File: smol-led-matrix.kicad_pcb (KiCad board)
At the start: 4 copper layers, 61.8 x 88.2 mm, 1139 parts, among them J1 USB_C_Receptacle_USB2.0, J2 TagConnect_TC2030_SWD, Q1 FS8205, Q2 AO3401A, SW1 SW_Push, SW2 SW_Push, U1 STM32L433CBTx, U2 TP4054, U3 DW01+G, U4 XC6206P332MR

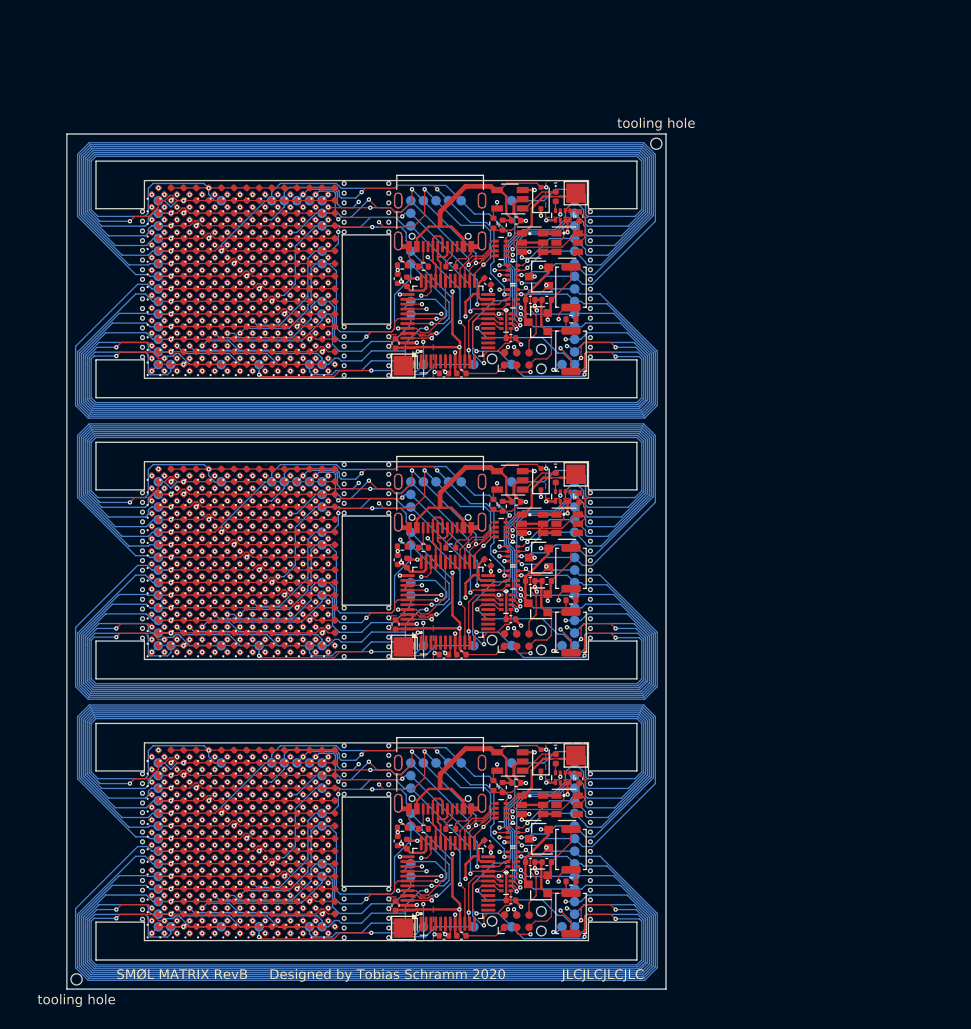
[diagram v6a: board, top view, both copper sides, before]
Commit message: Fix some clearance issues
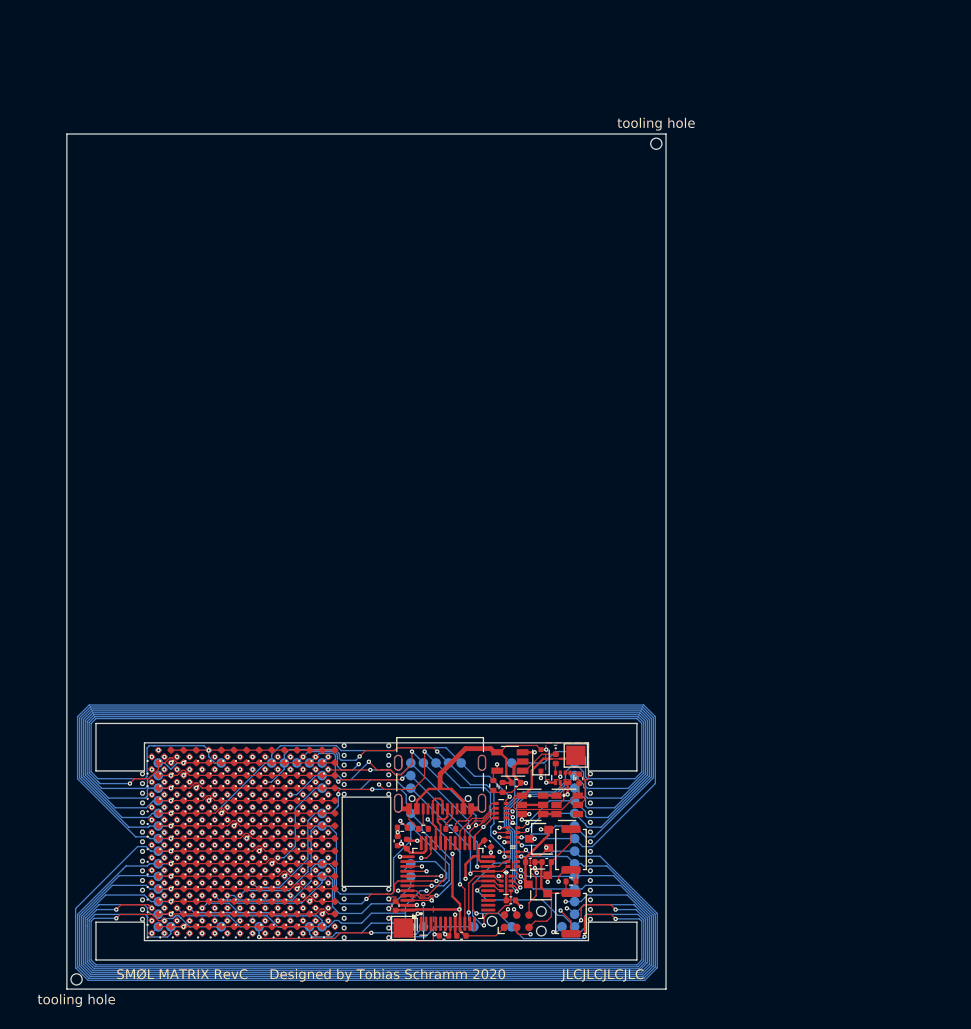
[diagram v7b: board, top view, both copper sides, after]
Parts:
- removed the C1 at (94.8, 86.5)
- removed the C1 at (94.8, 115.5)
- removed the C10 at (99.9, 82.8)
- removed the C10 at (99.9, 111.8)
- removed the C11 at (88.2, 76.7)
- removed the C11 at (88.2, 105.7)
- removed the C2 at (88.0, 83.4)
- removed the C2 at (88.0, 112.4)
- removed the C3 at (100.5, 70.7)
- removed the C3 at (100.5, 99.7)
- removed the C4 at (107.0, 70.3)
- removed the C4 at (107.0, 99.3)
- removed the C5 at (93.0, 86.5)
- removed the C5 at (93.0, 115.5)
- removed the C6 at (101.9, 78.9)
- removed the C6 at (101.9, 107.9)
- removed the C7 at (103.6, 78.9)
- removed the C7 at (103.6, 107.9)
- removed the C8 at (89.2, 77.0)
- removed the C8 at (89.2, 106.0)
- removed the C9 at (97.5, 77.0)
- removed the C9 at (97.5, 106.0)
- removed the D1 at (63.2, 67.7)
- removed the D1 at (63.2, 96.7)
- removed the D10 at (63.2, 79.4)
- removed the D10 at (63.2, 108.4)
- removed the D100 at (71.0, 79.4)
- removed the D100 at (71.0, 108.4)
- removed the D101 at (71.0, 80.7)
- removed the D101 at (71.0, 109.7)
- removed the D102 at (71.0, 82.0)
- removed the D102 at (71.0, 111.0)
- removed the D103 at (71.0, 83.3)
- removed the D103 at (71.0, 112.3)
- removed the D104 at (71.0, 84.6)
- removed the D104 at (71.0, 113.6)
- removed the D105 at (71.0, 85.9)
- removed the D105 at (71.0, 114.9)
- removed the D106 at (72.3, 67.7)
- removed the D106 at (72.3, 96.7)
- removed the D107 at (72.3, 69.0)
- removed the D107 at (72.3, 98.0)
- removed the D108 at (72.3, 70.3)
- removed the D108 at (72.3, 99.3)
- removed the D109 at (72.3, 71.6)
- removed the D109 at (72.3, 100.6)
- removed the D11 at (63.2, 80.7)
- removed the D11 at (63.2, 109.7)
- removed the D110 at (72.3, 72.9)
- removed the D110 at (72.3, 101.9)
- removed the D111 at (72.3, 74.2)
- removed the D111 at (72.3, 103.2)
- removed the D112 at (72.3, 75.5)
- removed the D112 at (72.3, 104.5)
- removed the D113 at (72.3, 76.8)
- removed the D113 at (72.3, 105.8)
- removed the D114 at (72.3, 78.1)
- removed the D114 at (72.3, 107.1)
- removed the D115 at (72.3, 79.4)
- removed the D115 at (72.3, 108.4)
- removed the D116 at (72.3, 80.7)
- removed the D116 at (72.3, 109.7)
- removed the D117 at (72.3, 82.0)
- removed the D117 at (72.3, 111.0)
- removed the D118 at (72.3, 83.3)
- removed the D118 at (72.3, 112.3)
- removed the D119 at (72.3, 84.6)
- removed the D119 at (72.3, 113.6)
- removed the D12 at (63.2, 82.0)
- removed the D12 at (63.2, 111.0)
- removed the D120 at (72.3, 85.9)
- removed the D120 at (72.3, 114.9)
- removed the D121 at (73.6, 67.7)
- removed the D121 at (73.6, 96.7)
- removed the D122 at (73.6, 69.0)
- removed the D122 at (73.6, 98.0)
- removed the D123 at (73.6, 70.3)
- removed the D123 at (73.6, 99.3)
- removed the D124 at (73.6, 71.6)
- removed the D124 at (73.6, 100.6)
- removed the D125 at (73.6, 72.9)
- removed the D125 at (73.6, 101.9)
- removed the D126 at (73.6, 74.2)
- removed the D126 at (73.6, 103.2)
- removed the D127 at (73.6, 75.5)
- removed the D127 at (73.6, 104.5)
- removed the D128 at (73.6, 76.8)
- removed the D128 at (73.6, 105.8)
- removed the D129 at (73.6, 78.1)
- removed the D129 at (73.6, 107.1)
- removed the D13 at (63.2, 83.3)
- removed the D13 at (63.2, 112.3)
- removed the D130 at (73.6, 79.4)
- removed the D130 at (73.6, 108.4)
- removed the D131 at (73.6, 80.7)
- removed the D131 at (73.6, 109.7)
- removed the D132 at (73.6, 82.0)
- removed the D132 at (73.6, 111.0)
- removed the D133 at (73.6, 83.3)
- removed the D133 at (73.6, 112.3)
- removed the D134 at (73.6, 84.6)
- removed the D134 at (73.6, 113.6)
- removed the D135 at (73.6, 85.9)
- removed the D135 at (73.6, 114.9)
- removed the D136 at (74.9, 67.7)
- removed the D136 at (74.9, 96.7)
- removed the D137 at (74.9, 69.0)
- removed the D137 at (74.9, 98.0)
- removed the D138 at (74.9, 70.3)
- removed the D138 at (74.9, 99.3)
- removed the D139 at (74.9, 71.6)
- removed the D139 at (74.9, 100.6)
- removed the D14 at (63.2, 84.6)
- removed the D14 at (63.2, 113.6)
- removed the D140 at (74.9, 72.9)
- removed the D140 at (74.9, 101.9)
- removed the D141 at (74.9, 74.2)
- removed the D141 at (74.9, 103.2)
- removed the D142 at (74.9, 75.5)
- removed the D142 at (74.9, 104.5)
- removed the D143 at (74.9, 76.8)
- removed the D143 at (74.9, 105.8)
- removed the D144 at (74.9, 78.1)
- removed the D144 at (74.9, 107.1)
- removed the D145 at (74.9, 79.4)
- removed the D145 at (74.9, 108.4)
- removed the D146 at (74.9, 80.7)
- removed the D146 at (74.9, 109.7)
- removed the D147 at (74.9, 82.0)
- removed the D147 at (74.9, 111.0)
- removed the D148 at (74.9, 83.3)
- removed the D148 at (74.9, 112.3)
- removed the D149 at (74.9, 84.6)
- removed the D149 at (74.9, 113.6)
- removed the D15 at (63.2, 85.9)
- removed the D15 at (63.2, 114.9)
- removed the D150 at (74.9, 85.9)
- removed the D150 at (74.9, 114.9)
- removed the D151 at (76.2, 67.7)
- removed the D151 at (76.2, 96.7)
- removed the D152 at (76.2, 69.0)
- removed the D152 at (76.2, 98.0)
- removed the D153 at (76.2, 70.3)
- removed the D153 at (76.2, 99.3)
- removed the D154 at (76.2, 71.6)
- removed the D154 at (76.2, 100.6)
- removed the D155 at (76.2, 72.9)
- removed the D155 at (76.2, 101.9)
- removed the D156 at (76.2, 74.2)
- removed the D156 at (76.2, 103.2)
- removed the D157 at (76.2, 75.5)
- removed the D157 at (76.2, 104.5)
- removed the D158 at (76.2, 76.8)
- removed the D158 at (76.2, 105.8)
- removed the D159 at (76.2, 78.1)
- removed the D159 at (76.2, 107.1)
- removed the D16 at (64.5, 67.7)
- removed the D16 at (64.5, 96.7)
- removed the D160 at (76.2, 79.4)
- removed the D160 at (76.2, 108.4)
- removed the D161 at (76.2, 80.7)
- removed the D161 at (76.2, 109.7)
- removed the D162 at (76.2, 82.0)
- removed the D162 at (76.2, 111.0)
- removed the D163 at (76.2, 83.3)
- removed the D163 at (76.2, 112.3)
- removed the D164 at (76.2, 84.6)
- removed the D164 at (76.2, 113.6)
- removed the D165 at (76.2, 85.9)
- removed the D165 at (76.2, 114.9)
- removed the D166 at (77.5, 67.7)
- removed the D166 at (77.5, 96.7)
- removed the D167 at (77.5, 69.0)
- removed the D167 at (77.5, 98.0)
- removed the D168 at (77.5, 70.3)
- removed the D168 at (77.5, 99.3)
- removed the D169 at (77.5, 71.6)
- removed the D169 at (77.5, 100.6)
- removed the D17 at (64.5, 69.0)
- removed the D17 at (64.5, 98.0)
- removed the D170 at (77.5, 72.9)
- removed the D170 at (77.5, 101.9)
- removed the D171 at (77.5, 74.2)
- removed the D171 at (77.5, 103.2)
- removed the D172 at (77.5, 75.5)
- removed the D172 at (77.5, 104.5)
- removed the D173 at (77.5, 76.8)
- removed the D173 at (77.5, 105.8)
- removed the D174 at (77.5, 78.1)
- removed the D174 at (77.5, 107.1)
- removed the D175 at (77.5, 79.4)
- removed the D175 at (77.5, 108.4)
- removed the D176 at (77.5, 80.7)
- removed the D176 at (77.5, 109.7)
- removed the D177 at (77.5, 82.0)
- removed the D177 at (77.5, 111.0)
- removed the D178 at (77.5, 83.3)
- removed the D178 at (77.5, 112.3)
- removed the D179 at (77.5, 84.6)
- removed the D179 at (77.5, 113.6)
- removed the D18 at (64.5, 70.3)
- removed the D18 at (64.5, 99.3)
- removed the D180 at (77.5, 85.9)
- removed the D180 at (77.5, 114.9)
- removed the D181 at (78.8, 67.7)
- removed the D181 at (78.8, 96.7)
- removed the D182 at (78.8, 69.0)
- removed the D182 at (78.8, 98.0)
- removed the D183 at (78.8, 70.3)
- removed the D183 at (78.8, 99.3)
- removed the D184 at (78.8, 71.6)
- removed the D184 at (78.8, 100.6)
- removed the D185 at (78.8, 72.9)
- removed the D185 at (78.8, 101.9)
- removed the D186 at (78.8, 74.2)
- removed the D186 at (78.8, 103.2)
- removed the D187 at (78.8, 75.5)
- removed the D187 at (78.8, 104.5)
- removed the D188 at (78.8, 76.8)
- removed the D188 at (78.8, 105.8)
- removed the D189 at (78.8, 78.1)
- removed the D189 at (78.8, 107.1)
- removed the D19 at (64.5, 71.6)
- removed the D19 at (64.5, 100.6)
- removed the D190 at (78.8, 79.4)
- removed the D190 at (78.8, 108.4)
- removed the D191 at (78.8, 80.7)
- removed the D191 at (78.8, 109.7)
- removed the D192 at (78.8, 82.0)
- removed the D192 at (78.8, 111.0)
- removed the D193 at (78.8, 83.3)
- removed the D193 at (78.8, 112.3)
- removed the D194 at (78.8, 84.6)
- removed the D194 at (78.8, 113.6)
- removed the D195 at (78.8, 85.9)
- removed the D195 at (78.8, 114.9)
- removed the D196 at (80.1, 67.7)
- removed the D196 at (80.1, 96.7)
- removed the D197 at (80.1, 69.0)
- removed the D197 at (80.1, 98.0)
- removed the D198 at (80.1, 70.3)
- removed the D198 at (80.1, 99.3)
- removed the D199 at (80.1, 71.6)
- removed the D199 at (80.1, 100.6)
- removed the D2 at (63.2, 69.0)
- removed the D2 at (63.2, 98.0)
- removed the D20 at (64.5, 72.9)
- removed the D20 at (64.5, 101.9)
- removed the D200 at (80.1, 72.9)
- removed the D200 at (80.1, 101.9)
- removed the D201 at (80.1, 74.2)
- removed the D201 at (80.1, 103.2)
- removed the D202 at (80.1, 75.5)
- removed the D202 at (80.1, 104.5)
- removed the D203 at (80.1, 76.8)
- removed the D203 at (80.1, 105.8)
- removed the D204 at (80.1, 78.1)
- removed the D204 at (80.1, 107.1)
- removed the D205 at (80.1, 79.4)
- removed the D205 at (80.1, 108.4)
- removed the D206 at (80.1, 80.7)
- removed the D206 at (80.1, 109.7)
- removed the D207 at (80.1, 82.0)
- removed the D207 at (80.1, 111.0)
- removed the D208 at (80.1, 83.3)
- removed the D208 at (80.1, 112.3)
- removed the D209 at (80.1, 84.6)
- removed the D209 at (80.1, 113.6)
- removed the D21 at (64.5, 74.2)
- removed the D21 at (64.5, 103.2)
- removed the D210 at (80.1, 85.9)
- removed the D210 at (80.1, 114.9)
- removed the D211 at (81.4, 67.7)
- removed the D211 at (81.4, 96.7)
- removed the D212 at (81.4, 69.0)
- removed the D212 at (81.4, 98.0)
- removed the D213 at (81.4, 70.3)
- removed the D213 at (81.4, 99.3)
- removed the D214 at (81.4, 71.6)
- removed the D214 at (81.4, 100.6)
- removed the D215 at (81.4, 72.9)
- removed the D215 at (81.4, 101.9)
- removed the D216 at (81.4, 74.2)
- removed the D216 at (81.4, 103.2)
- removed the D217 at (81.4, 75.5)
- removed the D217 at (81.4, 104.5)
- removed the D218 at (81.4, 76.8)
- removed the D218 at (81.4, 105.8)
- removed the D219 at (81.4, 78.1)
- removed the D219 at (81.4, 107.1)
- removed the D22 at (64.5, 75.5)
- removed the D22 at (64.5, 104.5)
- removed the D220 at (81.4, 79.4)
- removed the D220 at (81.4, 108.4)
- removed the D221 at (81.4, 80.7)
- removed the D221 at (81.4, 109.7)
- removed the D222 at (81.4, 82.0)
- removed the D222 at (81.4, 111.0)
- removed the D223 at (81.4, 83.3)
- removed the D223 at (81.4, 112.3)
- removed the D224 at (81.4, 84.6)
- removed the D224 at (81.4, 113.6)
- removed the D225 at (81.4, 85.9)
- removed the D225 at (81.4, 114.9)
- removed the D226 at (104.5, 68.2)
- removed the D226 at (104.5, 97.2)
- removed the D227 at (103.0, 68.4)
- removed the D227 at (103.0, 97.4)
- removed the D23 at (64.5, 76.8)
- removed the D23 at (64.5, 105.8)
- removed the D24 at (64.5, 78.1)
- removed the D24 at (64.5, 107.1)
- removed the D25 at (64.5, 79.4)
- removed the D25 at (64.5, 108.4)
- removed the D26 at (64.5, 80.7)
- removed the D26 at (64.5, 109.7)
- removed the D27 at (64.5, 82.0)
- removed the D27 at (64.5, 111.0)
- removed the D28 at (64.5, 83.3)
- removed the D28 at (64.5, 112.3)
- removed the D29 at (64.5, 84.6)
- removed the D29 at (64.5, 113.6)
- removed the D3 at (63.2, 70.3)
- removed the D3 at (63.2, 99.3)
- removed the D30 at (64.5, 85.9)
- removed the D30 at (64.5, 114.9)
- removed the D31 at (65.8, 67.7)
- removed the D31 at (65.8, 96.7)
- removed the D32 at (65.8, 69.0)
- removed the D32 at (65.8, 98.0)
- removed the D33 at (65.8, 70.3)
- removed the D33 at (65.8, 99.3)
- removed the D34 at (65.8, 71.6)
- removed the D34 at (65.8, 100.6)
- removed the D35 at (65.8, 72.9)
- removed the D35 at (65.8, 101.9)
- removed the D36 at (65.8, 74.2)
- removed the D36 at (65.8, 103.2)
- removed the D37 at (65.8, 75.5)
- removed the D37 at (65.8, 104.5)
- removed the D38 at (65.8, 76.8)
- removed the D38 at (65.8, 105.8)
- removed the D39 at (65.8, 78.1)
- removed the D39 at (65.8, 107.1)
- removed the D4 at (63.2, 71.6)
- removed the D4 at (63.2, 100.6)
- removed the D40 at (65.8, 79.4)
- removed the D40 at (65.8, 108.4)
- removed the D41 at (65.8, 80.7)
- removed the D41 at (65.8, 109.7)
- removed the D42 at (65.8, 82.0)
- removed the D42 at (65.8, 111.0)
- removed the D43 at (65.8, 83.3)
- removed the D43 at (65.8, 112.3)
- removed the D44 at (65.8, 84.6)
- removed the D44 at (65.8, 113.6)
- removed the D45 at (65.8, 85.9)
- removed the D45 at (65.8, 114.9)
- removed the D46 at (67.1, 67.7)
- removed the D46 at (67.1, 96.7)
- removed the D47 at (67.1, 69.0)
- removed the D47 at (67.1, 98.0)
- removed the D48 at (67.1, 70.3)
- removed the D48 at (67.1, 99.3)
- removed the D49 at (67.1, 71.6)
- removed the D49 at (67.1, 100.6)
- removed the D5 at (63.2, 72.9)
- removed the D5 at (63.2, 101.9)
- removed the D50 at (67.1, 72.9)
- removed the D50 at (67.1, 101.9)
- removed the D51 at (67.1, 74.2)
- removed the D51 at (67.1, 103.2)
- removed the D52 at (67.1, 75.5)
- removed the D52 at (67.1, 104.5)
- removed the D53 at (67.1, 76.8)
- removed the D53 at (67.1, 105.8)
- removed the D54 at (67.1, 78.1)
- removed the D54 at (67.1, 107.1)
- removed the D55 at (67.1, 79.4)
- removed the D55 at (67.1, 108.4)
- removed the D56 at (67.1, 80.7)
- removed the D56 at (67.1, 109.7)
- removed the D57 at (67.1, 82.0)
- removed the D57 at (67.1, 111.0)
- removed the D58 at (67.1, 83.3)
- removed the D58 at (67.1, 112.3)
- removed the D59 at (67.1, 84.6)
- removed the D59 at (67.1, 113.6)
- removed the D6 at (63.2, 74.2)
- removed the D6 at (63.2, 103.2)
- removed the D60 at (67.1, 85.9)
- removed the D60 at (67.1, 114.9)
- removed the D61 at (68.4, 67.7)
- removed the D61 at (68.4, 96.7)
- removed the D62 at (68.4, 69.0)
- removed the D62 at (68.4, 98.0)
- removed the D63 at (68.4, 70.3)
- removed the D63 at (68.4, 99.3)
- removed the D64 at (68.4, 71.6)
- removed the D64 at (68.4, 100.6)
- removed the D65 at (68.4, 72.9)
- removed the D65 at (68.4, 101.9)
- removed the D66 at (68.4, 74.2)
- removed the D66 at (68.4, 103.2)
- removed the D67 at (68.4, 75.5)
- removed the D67 at (68.4, 104.5)
- removed the D68 at (68.4, 76.8)
- removed the D68 at (68.4, 105.8)
- removed the D69 at (68.4, 78.1)
- removed the D69 at (68.4, 107.1)
- removed the D7 at (63.2, 75.5)
- removed the D7 at (63.2, 104.5)
- removed the D70 at (68.4, 79.4)
- removed the D70 at (68.4, 108.4)
- removed the D71 at (68.4, 80.7)
- removed the D71 at (68.4, 109.7)
- removed the D72 at (68.4, 82.0)
- removed the D72 at (68.4, 111.0)
- removed the D73 at (68.4, 83.3)
- removed the D73 at (68.4, 112.3)
- removed the D74 at (68.4, 84.6)
- removed the D74 at (68.4, 113.6)
- removed the D75 at (68.4, 85.9)
- removed the D75 at (68.4, 114.9)
- removed the D76 at (69.7, 67.7)
- removed the D76 at (69.7, 96.7)
- removed the D77 at (69.7, 69.0)
- removed the D77 at (69.7, 98.0)
- removed the D78 at (69.7, 70.3)
- removed the D78 at (69.7, 99.3)
- removed the D79 at (69.7, 71.6)
- removed the D79 at (69.7, 100.6)
- removed the D8 at (63.2, 76.8)
- removed the D8 at (63.2, 105.8)
- removed the D80 at (69.7, 72.9)
- removed the D80 at (69.7, 101.9)
- removed the D81 at (69.7, 74.2)
- removed the D81 at (69.7, 103.2)
- removed the D82 at (69.7, 75.5)
- removed the D82 at (69.7, 104.5)
- removed the D83 at (69.7, 76.8)
- removed the D83 at (69.7, 105.8)
- removed the D84 at (69.7, 78.1)
- removed the D84 at (69.7, 107.1)
- removed the D85 at (69.7, 79.4)
- removed the D85 at (69.7, 108.4)
- removed the D86 at (69.7, 80.7)
- removed the D86 at (69.7, 109.7)
- removed the D87 at (69.7, 82.0)
- removed the D87 at (69.7, 111.0)
- removed the D88 at (69.7, 83.3)
- removed the D88 at (69.7, 112.3)
- removed the D89 at (69.7, 84.6)
- removed the D89 at (69.7, 113.6)
- removed the D9 at (63.2, 78.1)
- removed the D9 at (63.2, 107.1)
- removed the D90 at (69.7, 85.9)
- removed the D90 at (69.7, 114.9)
- removed the D91 at (71.0, 67.7)
- removed the D91 at (71.0, 96.7)
- removed the D92 at (71.0, 69.0)
- removed the D92 at (71.0, 98.0)
- removed the D93 at (71.0, 70.3)
- removed the D93 at (71.0, 99.3)
- removed the D94 at (71.0, 71.6)
- removed the D94 at (71.0, 100.6)
- removed the D95 at (71.0, 72.9)
- removed the D95 at (71.0, 101.9)
- removed the D96 at (71.0, 74.2)
- removed the D96 at (71.0, 103.2)
- removed the D97 at (71.0, 75.5)
- removed the D97 at (71.0, 104.5)
- removed the D98 at (71.0, 76.8)
- removed the D98 at (71.0, 105.8)
- removed the D99 at (71.0, 78.1)
- removed the D99 at (71.0, 107.1)
- removed the J1 at (92.6, 70.9)
- removed the J1 at (92.6, 99.9)
- removed the J2 at (100.5, 85.0)
- removed the J2 at (100.5, 114.0)
- removed the Q1 at (102.1, 73.0)
- removed the Q1 at (102.1, 102.0)
- removed the Q2 at (102.8, 76.5)
- removed the Q2 at (102.8, 105.5)
- removed the R1 at (98.1, 71.0)
- removed the R1 at (98.1, 100.0)
- removed the R2 at (99.0, 71.2)
- removed the R2 at (99.0, 100.2)
- removed the R3 at (93.7, 75.5)
- removed the R3 at (93.7, 104.5)
- removed the R4 at (90.9, 75.5)
- removed the R4 at (90.9, 104.5)
- removed the R5 at (106.1, 80.9)
- removed the R5 at (106.1, 109.9)
- removed the R6 at (88.7, 75.3)
- removed the R6 at (88.7, 104.3)
- removed the REF** at (87.3, 66.9)
- removed the REF** at (87.3, 97.9)
- removed the REF** at (108.1, 98.8)
- removed the REF** at (61.9, 71.8)
- removed the REF** at (61.9, 100.8)
- removed the REF** at (108.1, 83.8)
- removed the REF** at (108.1, 112.8)
- removed the REF** at (108.1, 84.8)
- removed the REF** at (108.1, 113.8)
- removed the REF** at (108.1, 82.8)
- removed the REF** at (108.1, 111.8)
- removed the REF** at (108.1, 79.8)
- removed the REF** at (87.3, 67.9)
- removed the REF** at (108.1, 108.8)
- removed the REF** at (61.9, 73.8)
- removed the REF** at (61.9, 102.8)
- removed the REF** at (87.3, 96.9)
- removed the REF** at (82.7, 71.9)
- removed the REF** at (82.7, 100.9)
- removed the REF** at (108.1, 77.8)
- removed the REF** at (108.1, 106.8)
- removed the REF** at (108.1, 70.8)
- removed the REF** at (108.1, 99.8)
- removed the REF** at (82.7, 67.9)
- removed the REF** at (87.3, 95.9)
- removed the REF** at (82.7, 96.9)
- removed the REF** at (108.1, 71.8)
- removed the REF** at (108.1, 100.8)
- removed the REF** at (108.1, 72.8)
- removed the REF** at (108.1, 101.8)
- removed the REF** at (82.7, 84.7)
- removed the REF** at (82.7, 113.7)
- removed the REF** at (61.9, 78.8)
- removed the REF** at (61.9, 107.8)
- removed the REF** at (108.1, 78.8)
- removed the REF** at (87.3, 70.9)
- removed the REF** at (108.1, 107.8)
- removed the REF** at (82.7, 85.7)
- removed the REF** at (82.7, 114.7)
- removed the REF** at (61.9, 79.8)
- removed the REF** at (61.9, 108.8)
- removed the REF** at (87.3, 81.7)
- removed the REF** at (87.3, 110.7)
- removed the REF** at (61.9, 76.8)
- removed the REF** at (61.9, 105.8)
- removed the REF** at (108.1, 74.8)
- removed the REF** at (87.3, 99.9)
- removed the REF** at (108.1, 103.8)
- removed the REF** at (61.9, 75.8)
- removed the REF** at (61.9, 104.8)
- removed the REF** at (108.1, 76.8)
- removed the REF** at (108.1, 105.8)
- removed the REF** at (87.3, 85.7)
- removed the REF** at (87.3, 114.7)
- removed the REF** at (87.3, 84.7)
- removed the REF** at (87.3, 113.7)
- removed the REF** at (82.7, 66.9)
- removed the REF** at (108.1, 75.8)
- removed the REF** at (82.7, 95.9)
- removed the REF** at (82.7, 70.9)
- removed the REF** at (82.7, 99.9)
- removed the REF** at (82.7, 69.9)
- removed the REF** at (82.7, 98.9)
- removed the REF** at (82.7, 86.7)
- removed the REF** at (82.7, 115.7)
- removed the REF** at (87.3, 71.9)
- removed the REF** at (87.3, 100.9)
- removed the REF** at (87.3, 86.7)
- removed the REF** at (108.1, 104.8)
- removed the REF** at (87.3, 115.7)
- removed the REF** at (82.7, 81.7)
- removed the REF** at (82.7, 110.7)
- removed the REF** at (61.9, 70.8)
- removed the REF** at (61.9, 99.8)
- removed the REF** at (61.9, 77.8)
- removed the REF** at (61.9, 106.8)
- removed the REF** at (82.7, 68.9)
- removed the REF** at (82.7, 97.9)
- removed the REF** at (61.9, 82.8)
- removed the REF** at (87.3, 69.9)
- removed the REF** at (61.9, 111.8)
- removed the REF** at (87.3, 82.7)
- removed the REF** at (87.3, 111.7)
- removed the REF** at (108.1, 73.8)
- removed the REF** at (108.1, 102.8)
- removed the REF** at (87.3, 83.7)
- removed the REF** at (87.3, 112.7)
- removed the REF** at (61.9, 84.8)
- removed the REF** at (61.9, 113.8)
- removed the REF** at (108.1, 80.8)
- removed the REF** at (87.3, 98.9)
- removed the REF** at (108.1, 109.8)
- removed the REF** at (61.9, 74.8)
- removed the REF** at (61.9, 103.8)
- removed the REF** at (61.9, 83.8)
- removed the REF** at (61.9, 112.8)
- removed the REF** at (61.9, 80.8)
- removed the REF** at (61.9, 109.8)
- removed the REF** at (61.9, 81.8)
- removed the REF** at (61.9, 110.8)
- removed the REF** at (61.9, 69.8)
- removed the REF** at (87.3, 68.9)
- removed the REF** at (61.9, 98.8)
- removed the REF** at (82.7, 83.7)
- removed the REF** at (82.7, 112.7)
- removed the REF** at (108.1, 81.8)
- removed the REF** at (108.1, 110.8)
- removed the REF** at (82.7, 82.7)
- removed the REF** at (82.7, 111.7)
- removed the REF** at (61.9, 72.8)
- removed the REF** at (61.9, 101.8)
- removed the REF** at (108.1, 69.8)
- removed the RN1 at (99.4, 81.1)
- removed the RN1 at (99.4, 110.1)
- removed the RN2 at (105.2, 70.2)
- removed the RN2 at (105.2, 99.2)
- removed the RN3 at (100.1, 76.1)
- removed the RN3 at (100.1, 105.1)
- removed the RN4 at (100.1, 78.6)
- removed the RN4 at (100.1, 107.6)
- removed the RN5 at (98.9, 73.6)
- removed the RN5 at (98.9, 102.6)
- removed the SW1 at (106.1, 77.6)
- removed the SW1 at (106.1, 106.6)
- removed the SW2 at (106.1, 84.2)
- removed the SW2 at (106.1, 113.2)
- removed the TP1 at (106.6, 67.9)
- removed the TP1 at (106.6, 96.9)
- removed the TP10 at (63.5, 76.5)
- removed the TP10 at (63.5, 105.5)
- removed the TP11 at (63.5, 77.8)
- removed the TP11 at (63.5, 106.8)
- removed the TP12 at (63.5, 79.1)
- removed the TP12 at (63.5, 108.1)
- removed the TP13 at (63.5, 80.4)
- removed the TP13 at (63.5, 109.4)
- removed the TP14 at (63.5, 81.7)
- removed the TP14 at (63.5, 110.7)
- removed the TP15 at (63.5, 83.0)
- removed the TP15 at (63.5, 112.0)
- removed the TP16 at (63.5, 84.3)
- removed the TP16 at (63.5, 113.3)
- removed the TP17 at (64.8, 85.6)
- removed the TP17 at (64.8, 114.6)
- removed the TP18 at (63.5, 85.6)
- removed the TP18 at (63.5, 114.6)
- removed the TP19 at (70.0, 85.6)
- removed the TP19 at (70.0, 114.6)
- removed the TP2 at (88.8, 85.7)
- removed the TP2 at (88.8, 114.7)
- removed the TP20 at (73.9, 85.6)
- removed the TP20 at (73.9, 114.6)
- removed the TP21 at (79.1, 85.6)
- removed the TP21 at (79.1, 114.6)
- removed the TP22 at (80.4, 85.6)
- removed the TP22 at (80.4, 114.6)
- removed the TP23 at (80.4, 80.4)
- removed the TP23 at (80.4, 109.4)
- removed the TP24 at (80.4, 79.1)
- removed the TP24 at (80.4, 108.1)
- removed the TP25 at (80.4, 75.2)
- removed the TP25 at (80.4, 104.2)
- removed the TP26 at (80.4, 73.9)
- removed the TP26 at (80.4, 102.9)
- removed the TP27 at (76.5, 68.7)
- removed the TP27 at (76.5, 97.7)
- removed the TP28 at (80.4, 71.3)
- removed the TP28 at (80.4, 100.3)
- removed the TP29 at (80.4, 70.0)
- removed the TP29 at (80.4, 99.0)
- removed the TP3 at (70.0, 68.7)
- removed the TP3 at (70.0, 97.7)
- removed the TP30 at (77.8, 68.7)
- removed the TP30 at (77.8, 97.7)
- removed the TP31 at (79.1, 68.7)
- removed the TP31 at (79.1, 97.7)
- removed the TP32 at (80.4, 68.7)
- removed the TP32 at (80.4, 97.7)
- removed the TP33 at (75.2, 68.7)
- removed the TP33 at (75.2, 97.7)
- removed the TP34 at (100.0, 68.7)
- removed the TP34 at (100.0, 97.7)
- removed the TP35 at (106.5, 68.7)
- removed the TP35 at (106.5, 97.7)
- removed the TP36 at (106.5, 70.0)
- removed the TP36 at (106.5, 99.0)
- removed the TP37 at (106.5, 71.3)
- removed the TP37 at (106.5, 100.3)
- removed the TP38 at (106.5, 72.6)
- removed the TP38 at (106.5, 101.6)
- removed the TP39 at (106.5, 73.9)
- removed the TP39 at (106.5, 102.9)
- removed the TP4 at (63.5, 68.7)
- removed the TP4 at (63.5, 97.7)
- removed the TP40 at (106.5, 75.2)
- removed the TP40 at (106.5, 104.2)
- removed the TP41 at (106.5, 76.5)
- removed the TP41 at (106.5, 105.5)
- removed the TP42 at (106.5, 77.8)
- removed the TP42 at (106.5, 106.8)
- removed the TP43 at (106.5, 79.1)
- removed the TP43 at (106.5, 108.1)
- removed the TP44 at (106.5, 80.4)
- removed the TP44 at (106.5, 109.4)
- removed the TP45 at (106.5, 81.7)
- removed the TP45 at (106.5, 110.7)
- removed the TP46 at (106.5, 83.0)
- removed the TP46 at (106.5, 112.0)
- removed the TP47 at (106.5, 84.3)
- removed the TP47 at (106.5, 113.3)
- removed the TP48 at (105.2, 85.6)
- removed the TP48 at (105.2, 114.6)
- removed the TP49 at (106.5, 85.6)
- removed the TP49 at (106.5, 114.6)
- removed the TP5 at (63.5, 70.0)
- removed the TP5 at (63.5, 99.0)
- removed the TP50 at (100.0, 85.6)
- removed the TP50 at (100.0, 114.6)
- removed the TP51 at (96.1, 85.6)
- removed the TP51 at (96.1, 114.6)
- removed the TP52 at (90.9, 85.6)
- removed the TP52 at (90.9, 114.6)
- removed the TP53 at (89.6, 85.6)
- removed the TP53 at (89.6, 114.6)
- removed the TP54 at (89.6, 80.4)
- removed the TP54 at (89.6, 109.4)
- removed the TP55 at (89.6, 79.1)
- removed the TP55 at (89.6, 108.1)
- removed the TP56 at (89.6, 75.2)
- removed the TP56 at (89.6, 104.2)
- removed the TP57 at (89.6, 73.9)
- removed the TP57 at (89.6, 102.9)
- removed the TP58 at (93.5, 68.7)
- removed the TP58 at (93.5, 97.7)
- removed the TP59 at (89.6, 71.3)
- removed the TP59 at (89.6, 100.3)
- removed the TP6 at (63.5, 71.3)
- removed the TP6 at (63.5, 100.3)
- removed the TP60 at (89.6, 70.0)
- removed the TP60 at (89.6, 99.0)
- removed the TP61 at (92.2, 68.7)
- removed the TP61 at (92.2, 97.7)
- removed the TP62 at (90.9, 68.7)
- removed the TP62 at (90.9, 97.7)
- removed the TP63 at (89.6, 68.7)
- removed the TP63 at (89.6, 97.7)
- removed the TP64 at (94.8, 68.7)
- removed the TP64 at (94.8, 97.7)
- removed the TP7 at (63.5, 72.6)
- removed the TP7 at (63.5, 101.6)
- removed the TP8 at (63.5, 73.9)
- removed the TP8 at (63.5, 102.9)
- removed the TP9 at (63.5, 75.2)
- removed the TP9 at (63.5, 104.2)
- removed the U1 at (93.4, 81.1)
- removed the U1 at (93.4, 110.1)
- removed the U2 at (99.8, 68.5)
- removed the U2 at (99.8, 97.5)
- removed the U3 at (105.7, 73.0)
- removed the U3 at (105.7, 102.0)
- removed the U4 at (102.7, 81.2)
- removed the U4 at (102.7, 110.2)
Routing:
- net /A0: track 433.8 -> 144.9 mm, vias 6 -> 2
- net /A1: track 383.8 -> 127.9 mm, vias 9 -> 3
- net /A14: track 377.0 -> 125.4 mm, vias 9 -> 3
- net /K1: track 376.9 -> 125.6 mm, vias 57 -> 19
- net /A2: track 377.0 -> 125.8 mm, vias 6 -> 2
- net /A3: track 375.7 -> 125.4 mm, vias 6 -> 2
- net /A7: track 367.1 -> 122.4 mm, vias 6 -> 2
- net /A8: track 365.9 -> 122.0 mm, vias 6 -> 2
- net /A13: track 365.3 -> 121.7 mm, vias 9 -> 3
- net /A6: track 360.6 -> 120.2 mm, vias 6 -> 2
- net /A9: track 357.4 -> 118.5 mm, vias 6 -> 2
- net /A12: track 358.1 -> 119.4 mm, vias 9 -> 3
- net /A5: track 356.5 -> 118.8 mm, vias 6 -> 2
- net /K0: track 354.4 -> 118.1 mm, vias 57 -> 19
- net /A4: track 354.0 -> 118.0 mm, vias 6 -> 2
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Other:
- outline, holes or cut-outs redrawn
- board text added: "SMØL MATRIX RevC Designed by Tobias Schramm 2020"
- board text removed: "SMØL MATRIX RevB Designed by Tobias Schramm 2020"

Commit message: Add JLC order remarks
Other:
- board text added: "Add following remarks to order at JLC: 1. Please don't do trace width compensation 2. Please don't compensate size of annular rings"
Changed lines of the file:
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@@
   (general
     (thickness 1)
-    (drawings 31)
+    (drawings 32)
     (tracks 1871)
     (zones 0)
@@
     )
   )
+  (gr_text "Add following remarks to order at JLC:\n\n1. Please don't do trace width compensation\n2. Please don't compensate size of annular rings" (at 126.500001 80.3) (layer Cmts.User)
+    (effects (font (size 3 3) (thickness 0.45)) (justify left))
+  )
   (gr_text "SMØL MATRIX RevC     Designed by Tobias Schramm 2020" (at 79.300001 148.5) (layer F.SilkS)
